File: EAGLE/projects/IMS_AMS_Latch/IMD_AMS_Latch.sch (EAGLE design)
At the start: 3 parts, among them IC1 4071N

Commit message: Start new branch, for AMD/IMS schematic
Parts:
- added R2: (no value), rcl:R-EU_0207/15
- added R3: 2.2K, rcl:R-EU_0207/15
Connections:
- new net GND: R3.2
- net N$2: now also R3.1
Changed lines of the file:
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@@
 <part name="IMD" library="testpad" library_urn="urn:adsk.eagle:library:385" deviceset="TPS" device="PAD1-13" package3d_urn="urn:adsk.eagle:package:27946/1"/>
 <part name="IC1" library="40xx" library_urn="urn:adsk.eagle:library:80" deviceset="4071" device="N" package3d_urn="urn:adsk.eagle:package:820/2"/>
+<part name="R2" library="rcl" library_urn="urn:adsk.eagle:library:334" deviceset="R-EU_" device="0207/15" package3d_urn="urn:adsk.eagle:package:23492/1"/>
+<part name="R3" library="rcl" library_urn="urn:adsk.eagle:library:334" deviceset="R-EU_" device="0207/15" package3d_urn="urn:adsk.eagle:package:23492/1" value="2.2K"/>
+<part name="SUPPLY1" library="supply2" library_urn="urn:adsk.eagle:library:372" deviceset="GND" device=""/>
 </parts>
 <sheets>
@@
 <attribute name="VALUE" x="88.9" y="91.44" size="1.778" layer="96" rot="R90"/>
 </instance>
+<instance part="R2" gate="G$1" x="50.8" y="76.2" smashed="yes">
+<attribute name="NAME" x="46.99" y="77.6986" size="1.778" layer="95"/>
+<attribute name="VALUE" x="46.99" y="72.898" size="1.778" layer="96"/>
+</instance>
+<instance part="R3" gate="G$1" x="109.22" y="76.2" smashed="yes">
+<attribute name="NAME" x="105.41" y="77.6986" size="1.778" layer="95"/>
+<attribute name="VALUE" x="105.41" y="72.898" size="1.778" layer="96"/>
+</instance>
+<instance part="SUPPLY1" gate="GND" x="124.46" y="76.2" smashed="yes" rot="R90">
+<attribute name="VALUE" x="127.635" y="74.295" size="1.778" layer="96" rot="R90"/>
+</instance>
 </instances>
 <busses>
@@
 <segment>
 <pinref part="IMD" gate="G$1" pin="PP"/>
-<wire x1="93.98" y1="63.5" x2="93.98" y2="81.28" width="0.1524" layer="91"/>
+<wire x1="93.98" y1="63.5" x2="93.98" y2="76.2" width="0.1524" layer="91"/>
 <pinref part="IC1" gate="A" pin="I1"/>
+<wire x1="93.98" y1="76.2" x2="93.98" y2="81.28" width="0.1524" layer="91"/>
 <wire x1="93.98" y1="81.28" x2="86.36" y2="81.28" width="0.1524" layer="91"/>
+<pinref part="R3" gate="G$1" pin="1"/>
+<wire x1="104.14" y1="76.2" x2="93.98" y2="76.2" width="0.1524" layer="91"/>
+<junction x="93.98" y="76.2"/>
+</segment>
+</net>
+<net name="GND" class="0">
+<segment>
+<pinref part="SUPPLY1" gate="GND" pin="GND"/>
+<pinref part="R3" gate="G$1" pin="2"/>
+<wire x1="121.92" y1="76.2" x2="114.3" y2="76.2" width="0.1524" layer="91"/>
 </segment>
 </net>
@@
 packages will not be understood (or retained) with this version.
 </note>
+<note version="8.4" severity="warning">
+Since Version 8.4, EAGLE supports properties for SPICE simulation.
+Probes in schematics and SPICE mapping objects found in parts and library devices
+will not be understood with this version. Update EAGLE to the latest version
+for full support of SPICE simulation.
+</note>
 </compatibility>

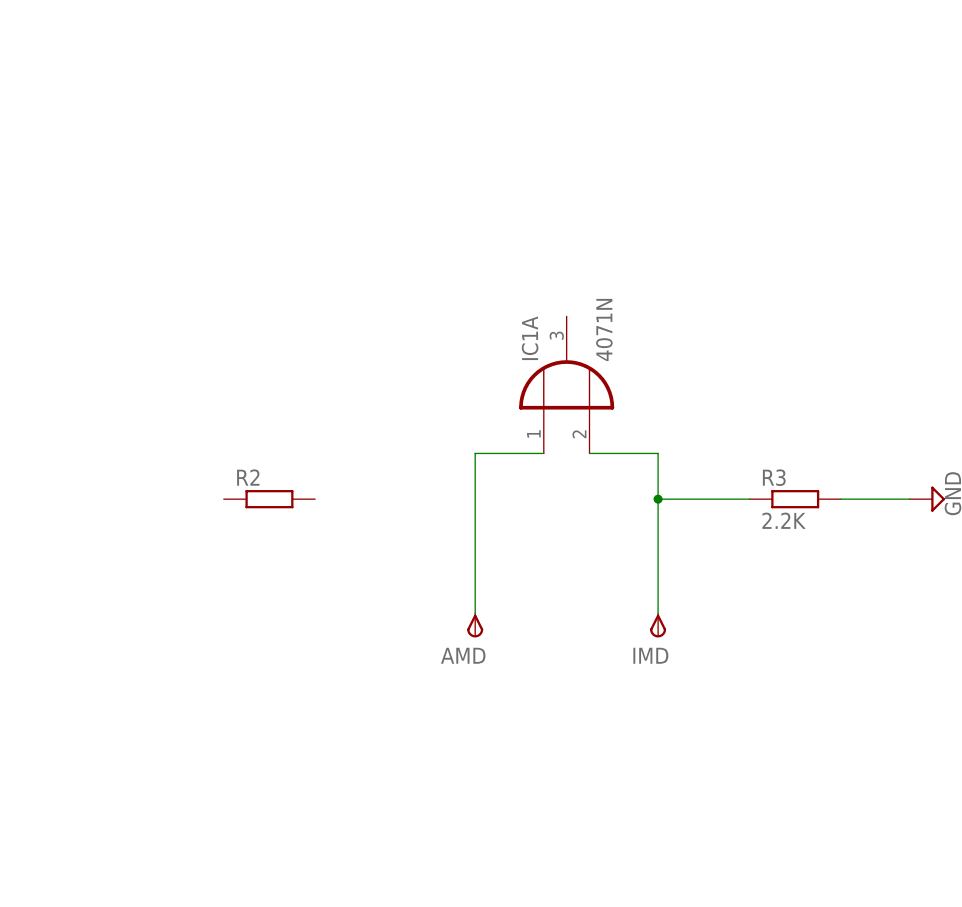
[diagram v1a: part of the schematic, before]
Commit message: addition of libraries and slight update to IMD_AMS_Latch.sch
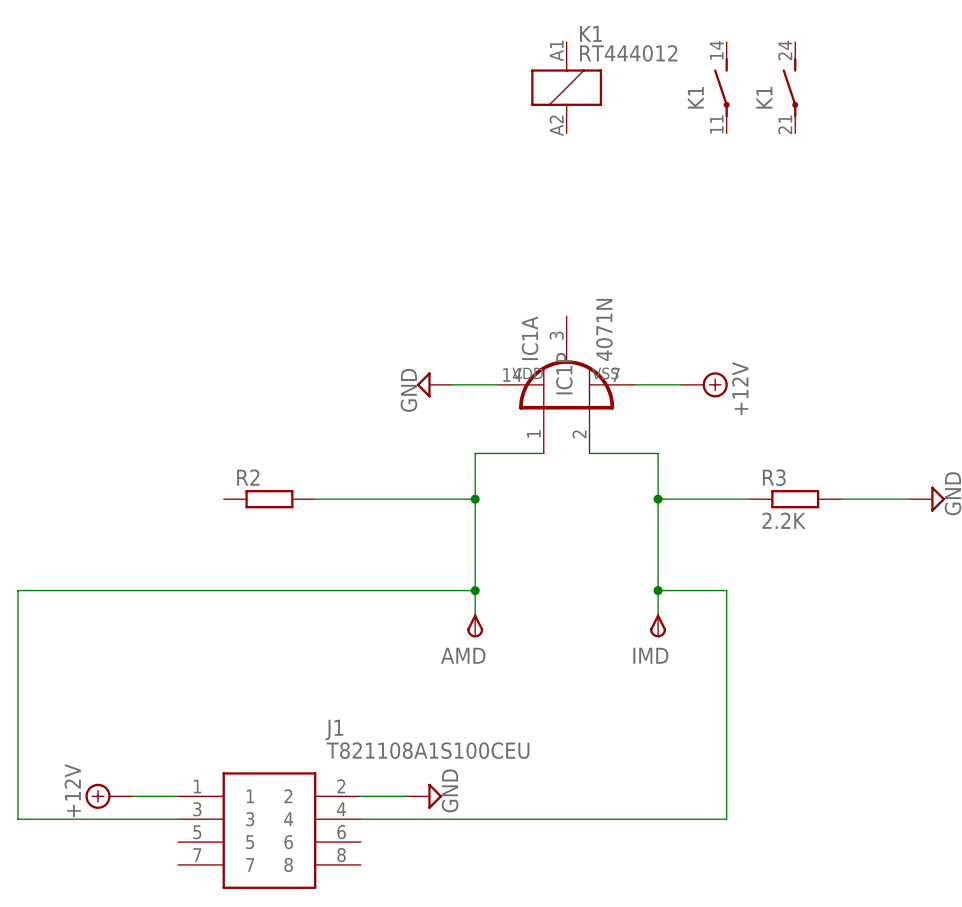
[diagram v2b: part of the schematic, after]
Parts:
- added J1: T821108A1S100CEU, T821108A1S100CEU:T821108A1S100CEU
- added K1: RT444012, relay:RT444012
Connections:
- new net +12V: IC1P.VSS, J1.1
- net GND: now also IC1P.VDD, J1.2
- net N$1: now also J1.3, R2.2
- net N$2: now also J1.4
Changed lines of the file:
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@@
 <part name="R3" library="rcl" library_urn="urn:adsk.eagle:library:334" deviceset="R-EU_" device="0207/15" package3d_urn="urn:adsk.eagle:package:23492/1" value="2.2K"/>
 <part name="SUPPLY1" library="supply2" library_urn="urn:adsk.eagle:library:372" deviceset="GND" device=""/>
+<part name="K1" library="relay" library_urn="urn:adsk.eagle:library:339" deviceset="RT44?*" device="4" package3d_urn="urn:adsk.eagle:package:24520/1" technology="012"/>
+<part name="J1" library="T821108A1S100CEU" deviceset="T821108A1S100CEU" device=""/>
+<part name="SUPPLY2" library="supply2" library_urn="urn:adsk.eagle:library:372" deviceset="GND" device=""/>
+<part name="SUPPLY3" library="supply2" library_urn="urn:adsk.eagle:library:372" deviceset="+12V" device=""/>
+<part name="SUPPLY4" library="supply2" library_urn="urn:adsk.eagle:library:372" deviceset="+12V" device=""/>
+<part name="SUPPLY5" library="supply2" library_urn="urn:adsk.eagle:library:372" deviceset="GND" device=""/>
 </parts>
 <sheets>
@@
 <attribute name="VALUE" x="127.635" y="74.295" size="1.778" layer="96" rot="R90"/>
 </instance>
+<instance part="K1" gate="1" x="83.82" y="121.92" smashed="yes">
+<attribute name="VALUE" x="85.09" y="124.841" size="1.778" layer="96"/>
+<attribute name="PART" x="85.09" y="127" size="1.778" layer="95"/>
+</instance>
+<instance part="K1" gate="2" x="101.6" y="121.92" smashed="yes">
+<attribute name="PART" x="99.06" y="119.38" size="1.778" layer="95" rot="R90"/>
+</instance>
+<instance part="K1" gate="3" x="109.22" y="121.92" smashed="yes">
+<attribute name="PART" x="106.68" y="119.38" size="1.778" layer="95" rot="R90"/>
+</instance>
+<instance part="J1" gate="G$1" x="40.64" y="43.18" smashed="yes">
+<attribute name="NAME" x="57.15" y="50.8" size="1.778" layer="95" align="center-left"/>
+<attribute name="VALUE" x="57.15" y="48.26" size="1.778" layer="96" align="center-left"/>
+</instance>
+<instance part="SUPPLY2" gate="GND" x="68.58" y="43.18" smashed="yes" rot="R90">
+<attribute name="VALUE" x="71.755" y="41.275" size="1.778" layer="96" rot="R90"/>
+</instance>
+<instance part="SUPPLY3" gate="+12V" x="33.02" y="43.18" smashed="yes" rot="R90">
+<attribute name="VALUE" x="29.845" y="40.64" size="1.778" layer="96" rot="R90"/>
+</instance>
+<instance part="IC1" gate="P" x="83.82" y="88.9" smashed="yes" rot="R90">
+<attribute name="NAME" x="84.455" y="87.63" size="1.778" layer="95" rot="R90"/>
+</instance>
+<instance part="SUPPLY4" gate="+12V" x="99.06" y="88.9" smashed="yes" rot="R270">
+<attribute name="VALUE" x="102.235" y="91.44" size="1.778" layer="96" rot="R270"/>
+</instance>
+<instance part="SUPPLY5" gate="GND" x="68.58" y="88.9" smashed="yes" rot="R270">
+<attribute name="VALUE" x="65.405" y="90.805" size="1.778" layer="96" rot="R270"/>
+</instance>
 </instances>
 <busses>
@@
 <pinref part="AMD" gate="G$1" pin="PP"/>
 <wire x1="81.28" y1="81.28" x2="73.66" y2="81.28" width="0.1524" layer="91"/>
-<wire x1="73.66" y1="81.28" x2="73.66" y2="63.5" width="0.1524" layer="91"/>
+<wire x1="73.66" y1="81.28" x2="73.66" y2="76.2" width="0.1524" layer="91"/>
+<pinref part="J1" gate="G$1" pin="3"/>
+<wire x1="73.66" y1="76.2" x2="73.66" y2="66.04" width="0.1524" layer="91"/>
+<wire x1="73.66" y1="66.04" x2="73.66" y2="63.5" width="0.1524" layer="91"/>
+<wire x1="40.64" y1="40.64" x2="22.86" y2="40.64" width="0.1524" layer="91"/>
+<wire x1="22.86" y1="40.64" x2="22.86" y2="66.04" width="0.1524" layer="91"/>
+<wire x1="22.86" y1="66.04" x2="73.66" y2="66.04" width="0.1524" layer="91"/>
+<junction x="73.66" y="66.04"/>
+<pinref part="R2" gate="G$1" pin="2"/>
+<wire x1="55.88" y1="76.2" x2="73.66" y2="76.2" width="0.1524" layer="91"/>
+<junction x="73.66" y="76.2"/>
 </segment>
 </net>
@@
 <segment>
 <pinref part="IMD" gate="G$1" pin="PP"/>
-<wire x1="93.98" y1="63.5" x2="93.98" y2="76.2" width="0.1524" layer="91"/>
+<wire x1="93.98" y1="63.5" x2="93.98" y2="66.04" width="0.1524" layer="91"/>
 <pinref part="IC1" gate="A" pin="I1"/>
+<wire x1="93.98" y1="66.04" x2="93.98" y2="76.2" width="0.1524" layer="91"/>
 <wire x1="93.98" y1="76.2" x2="93.98" y2="81.28" width="0.1524" layer="91"/>
 <wire x1="93.98" y1="81.28" x2="86.36" y2="81.28" width="0.1524" layer="91"/>
@@
 <wire x1="104.14" y1="76.2" x2="93.98" y2="76.2" width="0.1524" layer="91"/>
 <junction x="93.98" y="76.2"/>
+<pinref part="J1" gate="G$1" pin="4"/>
+<wire x1="60.96" y1="40.64" x2="101.6" y2="40.64" width="0.1524" layer="91"/>
+<wire x1="101.6" y1="40.64" x2="101.6" y2="66.04" width="0.1524" layer="91"/>
+<wire x1="101.6" y1="66.04" x2="93.98" y2="66.04" width="0.1524" layer="91"/>
+<junction x="93.98" y="66.04"/>
 </segment>
 </net>
@@
 <wire x1="121.92" y1="76.2" x2="114.3" y2="76.2" width="0.1524" layer="91"/>
 </segment>
+<segment>
+<pinref part="J1" gate="G$1" pin="2"/>
+<pinref part="SUPPLY2" gate="GND" pin="GND"/>
+<wire x1="60.96" y1="43.18" x2="66.04" y2="43.18" width="0.1524" layer="91"/>
+</segment>
+<segment>
+<pinref part="SUPPLY5" gate="GND" pin="GND"/>
+<pinref part="IC1" gate="P" pin="VDD"/>
+<wire x1="71.12" y1="88.9" x2="76.2" y2="88.9" width="0.1524" layer="91"/>
+</segment>
 </net>
+<net name="+12V" class="0">
+<segment>
+<pinref part="SUPPLY3" gate="+12V" pin="+12V"/>
+<pinref part="J1" gate="G$1" pin="1"/>
+<wire x1="35.56" y1="43.18" x2="40.64" y2="43.18" width="0.1524" layer="91"/>
+</segment>
+<segment>
+<pinref part="IC1" gate="P" pin="VSS"/>
+<pinref part="SUPPLY4" gate="+12V" pin="+12V"/>
+<wire x1="91.44" y1="88.9" x2="96.52" y2="88.9" width="0.1524" layer="91"/>
+</segment>
+</net>

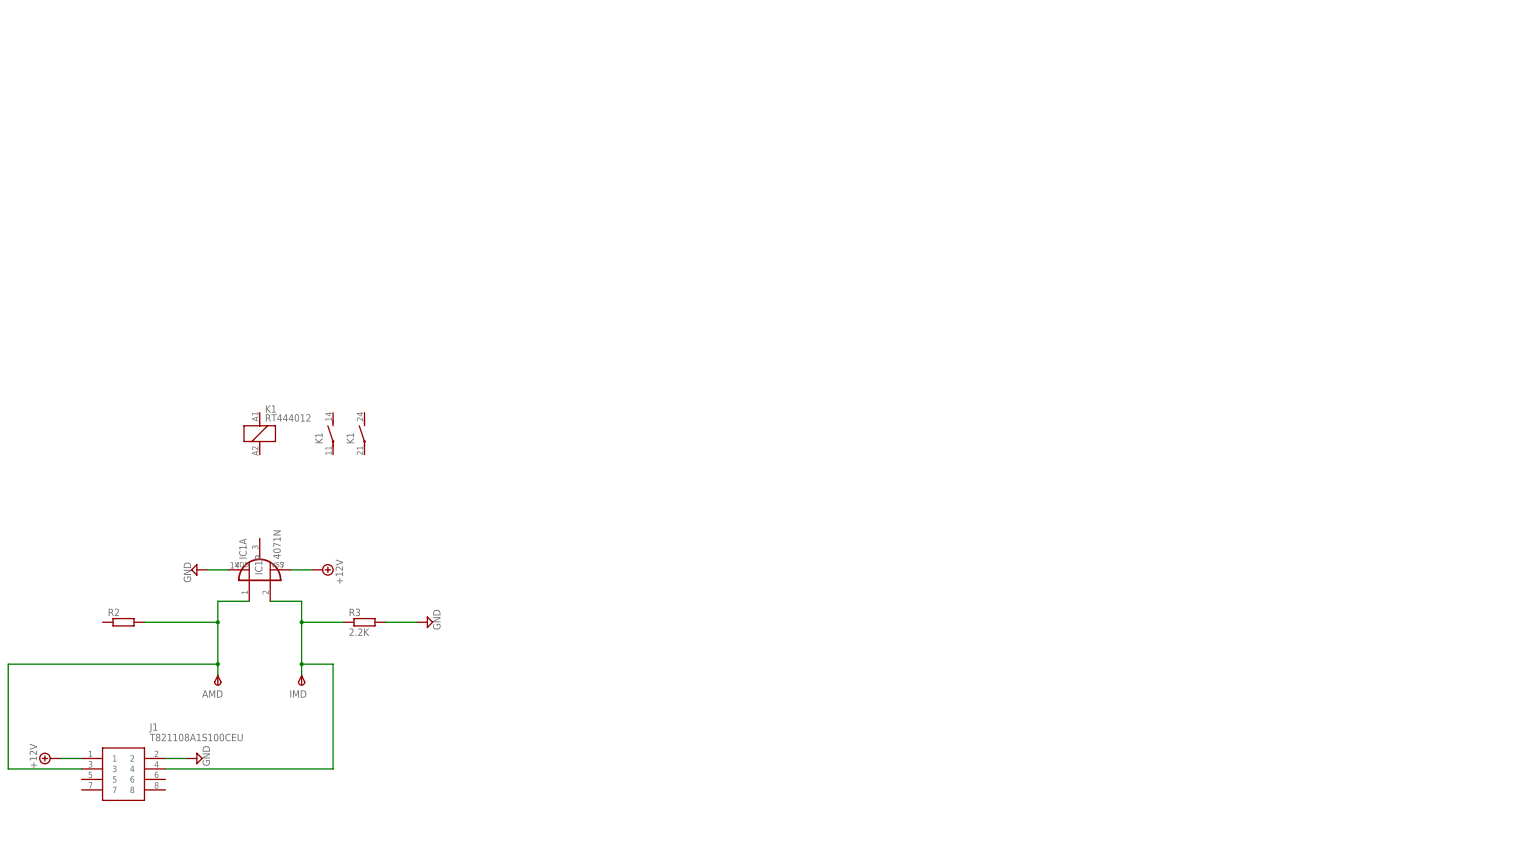
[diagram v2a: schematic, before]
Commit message: Completion of AMS/IMD latch schematic
Signed-off-by: Jack Bruford <jack.bruford41@gmail.com>
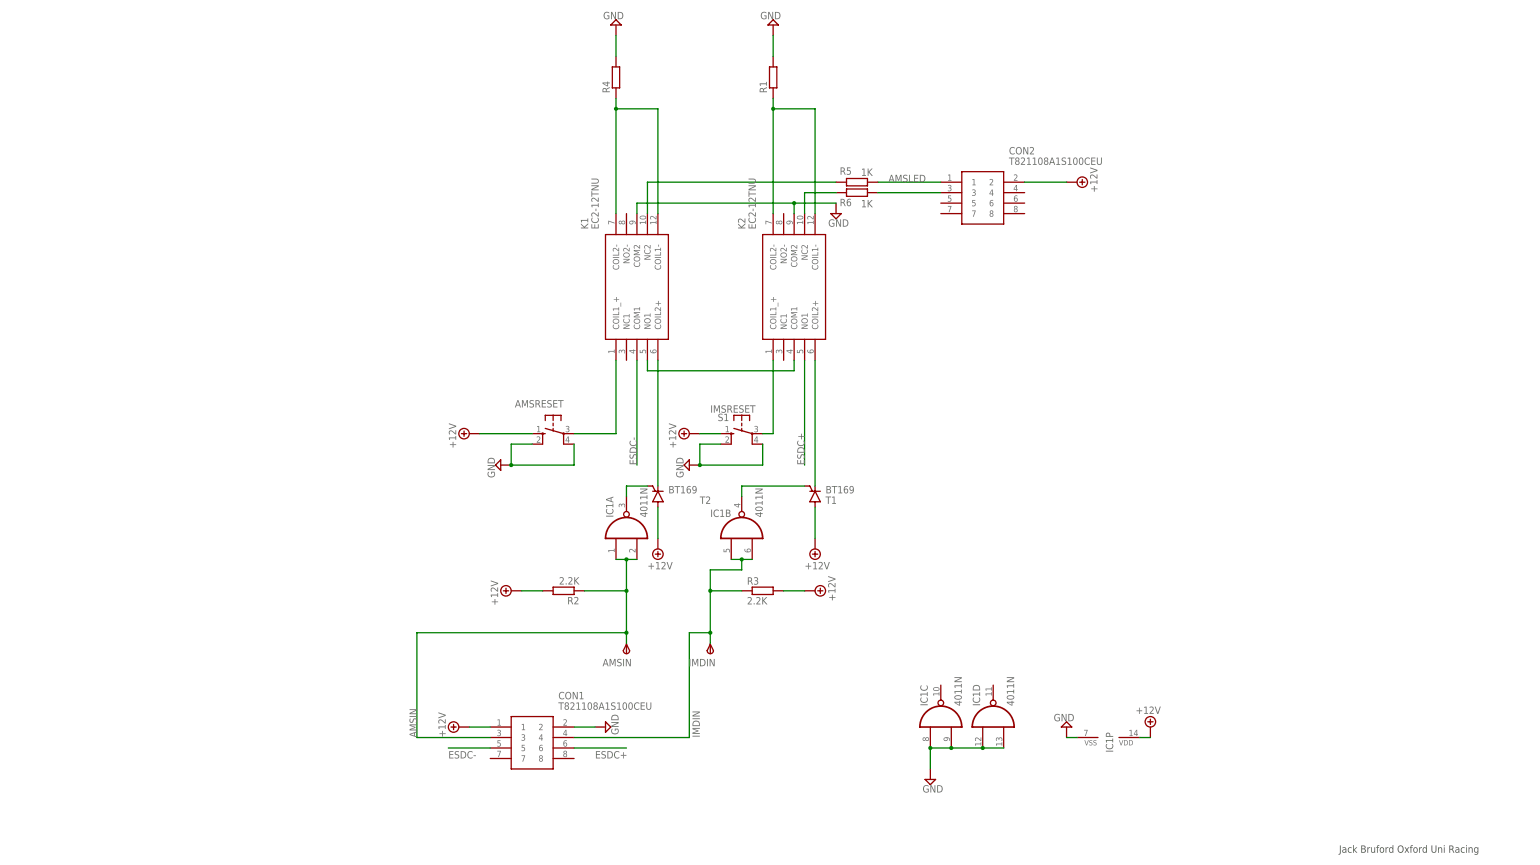
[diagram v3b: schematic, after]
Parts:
- removed AMD, IMD: TPSPAD1-13, testpad:TPSPAD1-13
- removed J1: T821108A1S100CEU, T821108A1S100CEU:T821108A1S100CEU
- added AMSIN, IMDIN: TPSPAD1-13, testpad:TPSPAD1-13
- added AMSRESET, S1: (no value), switch-omron:10-XX
- added CON1, CON2: T821108A1S100CEU, T821108A1S100CEU:T821108A1S100CEU
- added K2: EC2-12TNU, SamacSys_Parts:EC2-12TNU
- added R1, R4: (no value), rcl:R-EU_0207/15
- added R5, R6: 1K, rcl:R-EU_0207/15
- added T1, T2: BT169, triac:BT169
- IC1: value 4071N -> 4011N; device 40xx:4071N -> 40xx:4011N
- K1: value RT444012 -> EC2-12TNU; device relay:RT444012 -> SamacSys_Parts:EC2-12TNU
- R2: value (none) -> 2.2K
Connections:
- new net AMSIN: AMSIN.PP, CON1.3, IC1A.I0, IC1A.I1, R2.1
- new net AMSLED: K1.NC2, R5.2
- new net ESDC+: CON1.6, K2.NO1
- new net ESDC-: CON1.5, K1.COM1
- new net IMDIN: CON1.4, IC1B.I0, IC1B.I1, IMDIN.PP, R3.1
- new net IMSRESET: K1.NO1, K2.COM1
- new net N$10: IC1A.O, T2.G
- new net N$11: IC1B.O, T1.G
- new net N$3: K2.COIL1-, K2.COIL2-, R1.1
- new net N$4: K2.COIL2+, T1.C
- new net N$5: K2.COIL1_+, S1.P
- new net N$6: K1.COIL1-, K1.COIL2-, R4.1
- new net N$7: K2.NC2, R6.2
- new net N$8: CON2.1, R5.1
- new net N$9: CON2.3, R6.1
- net +12V: now also AMSRESET.S, CON1.1, CON2.2, IC1P.VDD, R2.2, R3.2, S1.S, T1.A, T2.A; no longer IC1P.VSS, J1.1
- net GND: now also AMSRESET.P1, AMSRESET.S1, CON1.2, IC1C.I0, IC1C.I1, IC1D.I0, IC1D.I1, IC1P.VSS, K1.COM2, K2.COM2, R1.2, R4.2, S1.P1, S1.S1; no longer IC1P.VDD, J1.2, R3.2
- net N$1: now also AMSRESET.P, K1.COIL1_+; no longer AMD.PP, IC1A.I0, J1.3, R2.2
- net N$2: now also K1.COIL2+, T2.C; no longer IC1A.I1, IMD.PP, J1.4, R3.1
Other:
- note added: "Jack Bruford Oxford Uni Racing"
- moved on the sheet: IC1P, R2, R3
